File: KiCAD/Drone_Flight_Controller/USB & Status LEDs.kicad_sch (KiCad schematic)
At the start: 25 parts, among them P701 USB_C_Plug_USB2.0, Q701 BC846C, Q702 BC846C, Q703 BC846C, Q704 BC846C, Q705 BC846C, Q706 BC846C, Q707 BC846C, U701 MCP2200-I-SO, Y701 CSTNE12M0GH5L000R0

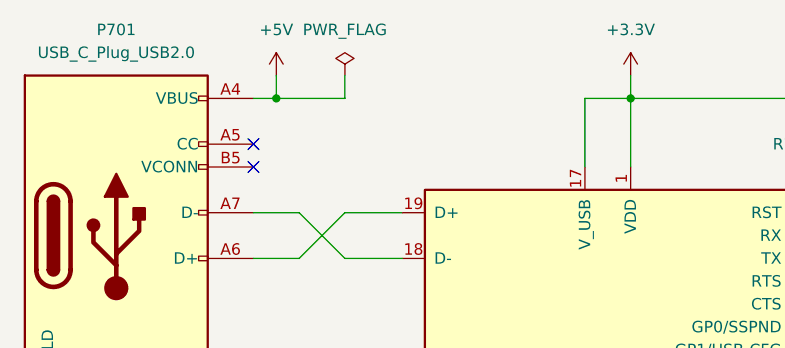
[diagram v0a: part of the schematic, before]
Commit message: Add +4V76 via BEC circuits and USB
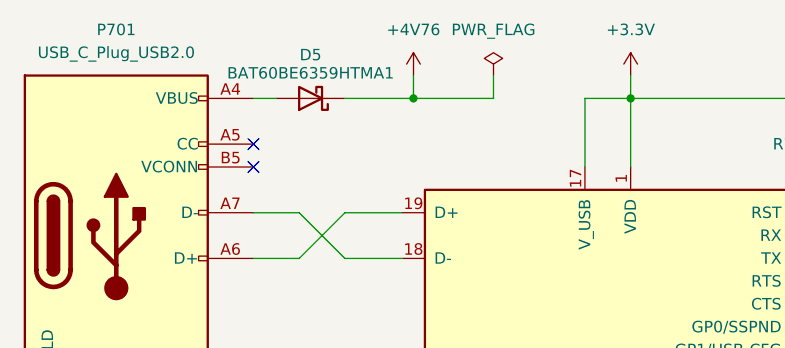
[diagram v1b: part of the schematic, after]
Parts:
- added D5: BAT60BE6359HTMA1, Diode_SMD:D_SOD-323F, symbol Device:D_Schottky
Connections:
- net +5V: no longer P701.A4 (VBUS), P701.A9 (VBUS), P701.B4 (VBUS), P701.B9 (VBUS)
- new net: D5.2 (A), P701.A4 (VBUS), P701.A9 (VBUS), P701.B4 (VBUS), P701.B9 (VBUS)
- new net +4V76: D5.1 (K)

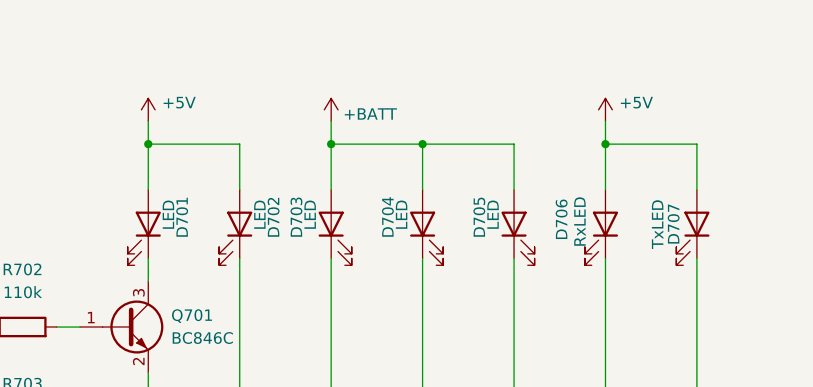
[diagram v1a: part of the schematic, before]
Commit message: Change 5V to 4V76
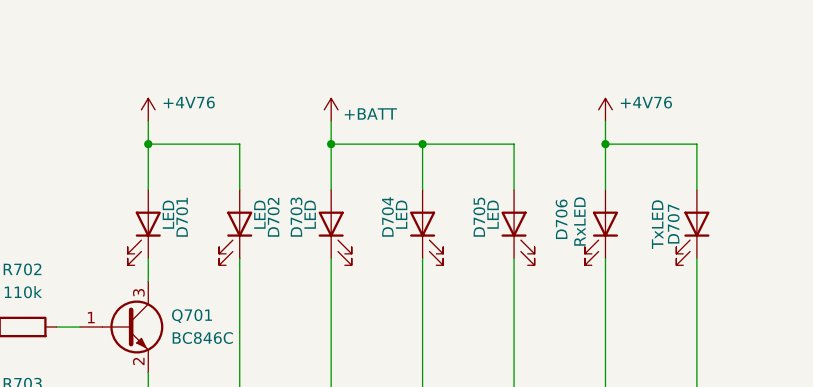
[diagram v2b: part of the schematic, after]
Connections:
- net +5V is gone; now on net +4V76: D701.2 (A), D702.2 (A), D706.2 (A), D707.2 (A)
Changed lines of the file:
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@@
 			)
 		)
-		(property "Value" "+5V"
+		(property "Value" "+4V76"
 			(at 199.644 46.228 0)
 			(effects
@@
 	)
 	(symbol
+		(lib_id "power:+5V")
+		(at 248.92 48.26 0)
+		(mirror y)
+		(unit 1)
+		(exclude_from_sim no)
+		(in_bom yes)
+		(on_board yes)
+		(dnp no)
+		(property "Reference" "#PWR05"
+			(at 248.92 52.07 0)
+			(effects
+				(font
+					(size 1.27 1.27)
+				)
+				(hide yes)
+			)
+		)
+		(property "Value" "+4V76"
+			(at 250.444 46.228 0)
+			(effects
+				(font
+					(size 1.27 1.27)
+				)
+				(justify right)
+			)
+		)
+		(property "Footprint" ""
+			(at 248.92 48.26 0)
+			(effects
+				(font
+					(size 1.27 1.27)
+				)
+				(hide yes)
+			)
+		)
+		(property "Datasheet" ""
+			(at 248.92 48.26 0)
+			(effects
+				(font
+					(size 1.27 1.27)
+				)
+				(hide yes)
+			)
+		)
+		(property "Description" "Power symbol creates a global label with name \"+5V\""
+			(at 248.92 48.26 0)
+			(effects
+				(font
+					(size 1.27 1.27)
+				)
+				(hide yes)
+			)
+		)
+		(pin "1"
+		)
+		(instances
+			(project "Drone_Flight_Controller"
+				(path "/05daaa24-e506-4b9a-9564-8bf799413ca8/8421779c-d2a0-463b-acfb-bef6fd845f5d"
+					(reference "#PWR05")
+					(unit 1)
+				)
+			)
+		)
+	)
+	(symbol
 		(lib_id "power:-BATT")
 		(at 218.44 157.48 180)
@@
 					(unit 1)
 				)
-			)
-		)
-	)
-	(symbol
-		(lib_id "power:+5V")
-		(at 248.92 48.26 0)
-		(mirror y)
-		(unit 1)
-		(exclude_from_sim no)
-		(in_bom yes)
-		(on_board yes)
-		(dnp no)
-		(property "Reference" "#PWR0705"
-			(at 248.92 52.07 0)
-			(effects
-				(font
-					(size 1.27 1.27)
-				)
-				(hide yes)
-			)
-		)
-		(property "Value" "+5V"
-			(at 250.444 46.228 0)
-			(effects
-				(font
-					(size 1.27 1.27)
-				)
-				(justify right)
-			)
-		)
-		(property "Footprint" ""
-			(at 248.92 48.26 0)
-			(effects
-				(font
-					(size 1.27 1.27)
-				)
-				(hide yes)
-			)
-		)
-		(property "Datasheet" ""
-			(at 248.92 48.26 0)
-			(effects
-				(font
-					(size 1.27 1.27)
-				)
-				(hide yes)
-			)
-		)
-		(property "Description" "Power symbol creates a global label with name \"+5V\""
-			(at 248.92 48.26 0)
-			(effects
-				(font
-					(size 1.27 1.27)
-				)
-				(hide yes)
-			)
-		)
-		(pin "1"
-		)
-		(instances
-			(project "Drone_Flight_Controller"
-				(path "/05daaa24-e506-4b9a-9564-8bf799413ca8/8421779c-d2a0-463b-acfb-bef6fd845f5d"
-					(reference "#PWR0705")
-					(unit 1)
-				)

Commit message: Reannotate
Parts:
- renumbered D5 to D601, D701 to D602, D702 to D603, D703 to D604, D704 to D605, D705 to D606, D706 to D607, D707 to D608, P701 to P601, Q701 to Q601, Q702 to Q602, Q703 to Q603, Q704 to Q604, Q705 to Q605, Q706 to Q606, Q707 to Q607, R701 to R601, R702 to R602, R703 to R603, R704 to R604, R705 to R605, R706 to R606, R707 to R607, R708 to R608, U701 to U601, Y701 to Y601

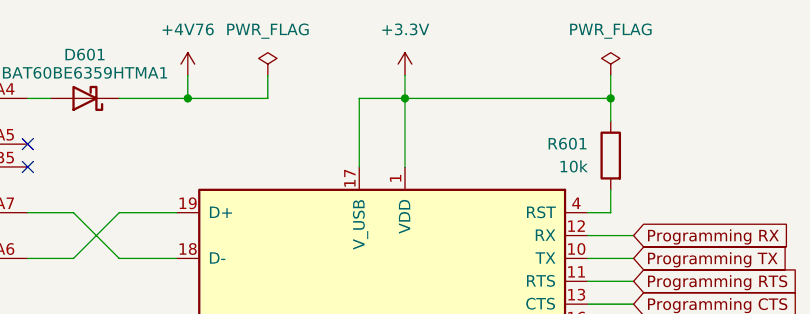
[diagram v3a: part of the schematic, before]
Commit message: Change "+3.3V" to "+3V3" for consistency
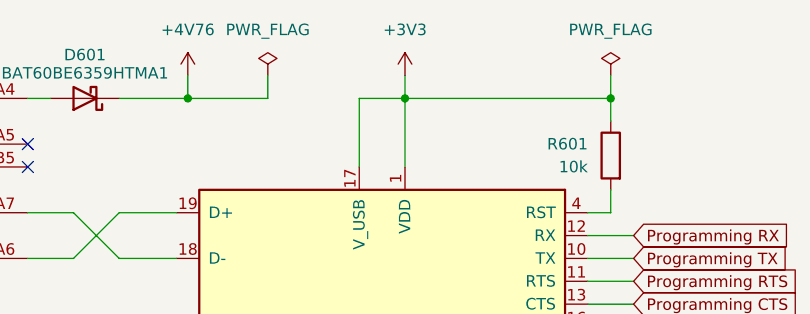
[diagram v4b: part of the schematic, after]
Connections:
- net +3.3V renamed +3V3
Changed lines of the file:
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@@
 	(title_block
 		(title "USB & Status LEDs")
-		(date "2025-09-12")
+		(date "2025-09-19")
 		(rev "V2")
 		(company "HTL Steyr")
@@
 		(dnp no)
 		(fields_autoplaced yes)
-		(property "Reference" "#PWR0602"
+		(property "Reference" "+3V3"
 			(at 133.35 46.99 0)
 			(effects
@@
 			)
 		)
-		(property "Value" "+3.3V"
+		(property "Value" "+3V3"
 			(at 133.35 38.1 0)
 			(effects
@@
 			(project ""
 				(path "/05daaa24-e506-4b9a-9564-8bf799413ca8/8421779c-d2a0-463b-acfb-bef6fd845f5d"
-					(reference "#PWR0602")
+					(reference "+3V3")
 					(unit 1)
 				)
